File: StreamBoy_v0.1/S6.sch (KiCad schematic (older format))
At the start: 24 parts, among them U1 XC6SLX9-TQG144

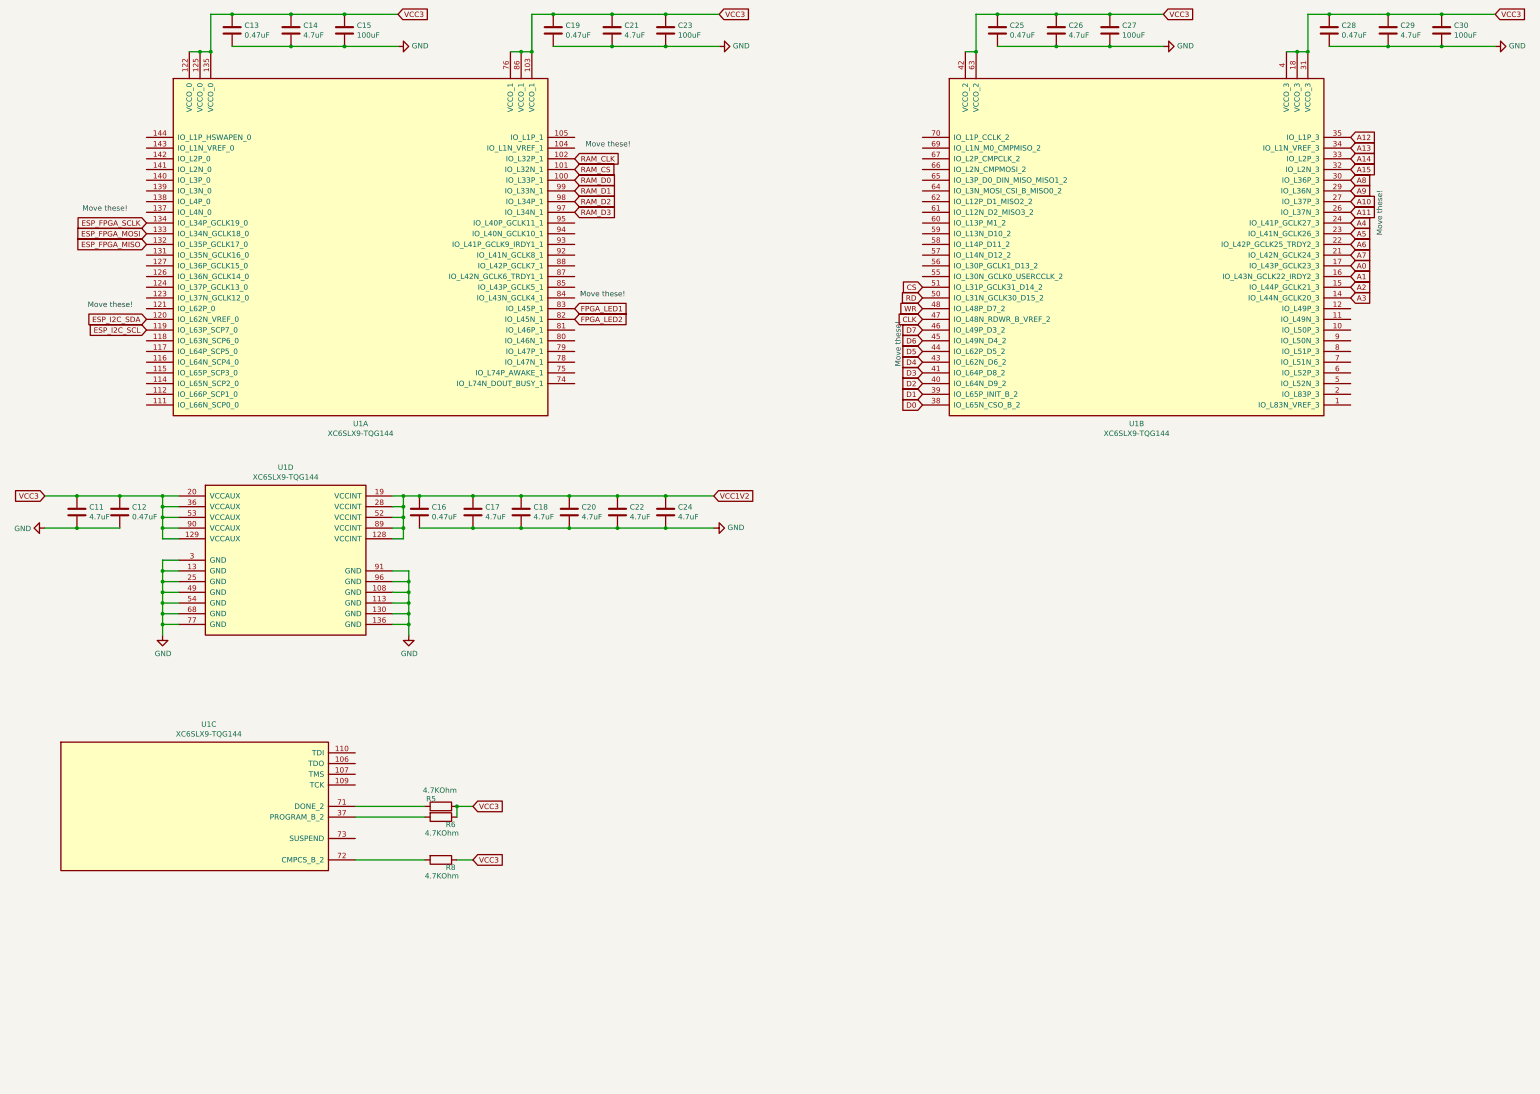
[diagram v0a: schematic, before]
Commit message: Added most stuff to fpga
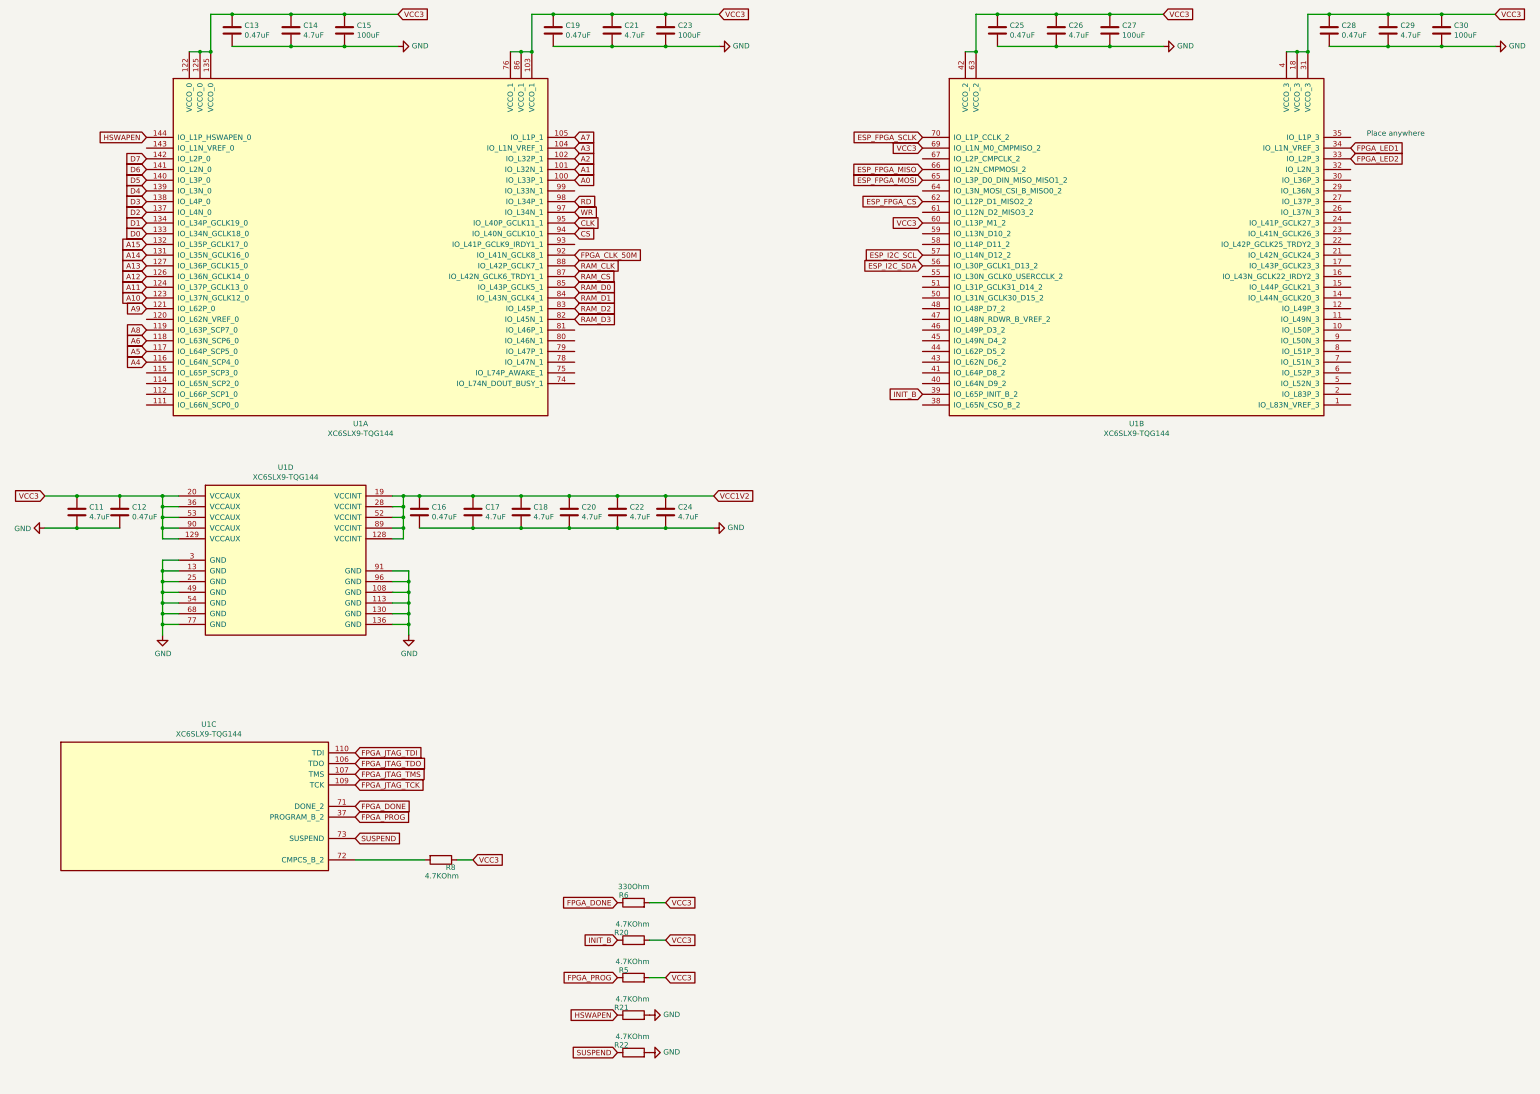
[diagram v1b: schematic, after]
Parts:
- added R20, R21, R22: 4.7KOhm, Resistor_SMD:R_0805_2012Metric, symbol Device:R
- C11, C12, C13, C14, C15, C16, C17, C18, C19, C20, C21, C22, C23, C24, C25, C26, C27, C28, C29, C30: footprint Capacitor_SMD:C_0805_2012Metric -> Capacitor_SMD:C_0402_1005Metric
- R6: value 4.7KOhm -> 330Ohm
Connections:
- net A0: now also U1.100 (IO_L33P_1); no longer U1.17 (IO_L43P_GCLK23_3)
- net A1: now also U1.101 (IO_L32N_1); no longer U1.16 (IO_L43N_GCLK22_IRDY2_3)
- net A10: now also U1.123 (IO_L37N_GCLK12_0); no longer U1.27 (IO_L37P_3)
- net A11: now also U1.124 (IO_L37P_GCLK13_0); no longer U1.26 (IO_L37N_3)
- net A12: now also U1.126 (IO_L36N_GCLK14_0); no longer U1.35 (IO_L1P_3)
- net A13: now also U1.127 (IO_L36P_GCLK15_0); no longer U1.34 (IO_L1N_VREF_3)
- net A14: now also U1.131 (IO_L35N_GCLK16_0); no longer U1.33 (IO_L2P_3)
- net A15: now also U1.132 (IO_L35P_GCLK17_0); no longer U1.32 (IO_L2N_3)
- net A2: now also U1.102 (IO_L32P_1); no longer U1.15 (IO_L44P_GCLK21_3)
- net A3: now also U1.104 (IO_L1N_VREF_1); no longer U1.14 (IO_L44N_GCLK20_3)
- net A4: now also U1.116 (IO_L64N_SCP4_0); no longer U1.24 (IO_L41P_GCLK27_3)
- net A5: now also U1.117 (IO_L64P_SCP5_0); no longer U1.23 (IO_L41N_GCLK26_3)
- net A6: now also U1.118 (IO_L63N_SCP6_0); no longer U1.22 (IO_L42P_GCLK25_TRDY2_3)
- net A7: now also U1.105 (IO_L1P_1); no longer U1.21 (IO_L42N_GCLK24_3)
- net A8: now also U1.119 (IO_L63P_SCP7_0); no longer U1.30 (IO_L36P_3)
- net A9: now also U1.121 (IO_L62P_0); no longer U1.29 (IO_L36N_3)
- net CLK: now also U1.95 (IO_L40P_GCLK11_1); no longer U1.47 (IO_L48N_RDWR_B_VREF_2)
- net CS: now also U1.94 (IO_L40N_GCLK10_1); no longer U1.51 (IO_L31P_GCLK31_D14_2)
- net D0: now also U1.133 (IO_L34N_GCLK18_0); no longer U1.38 (IO_L65N_CSO_B_2)
- net D1: now also U1.134 (IO_L34P_GCLK19_0); no longer U1.39 (IO_L65P_INIT_B_2)
- net D2: now also U1.137 (IO_L4N_0); no longer U1.40 (IO_L64N_D9_2)
- net D3: now also U1.138 (IO_L4P_0); no longer U1.41 (IO_L64P_D8_2)
- net D4: now also U1.139 (IO_L3N_0); no longer U1.43 (IO_L62N_D6_2)
- net D5: now also U1.140 (IO_L3P_0); no longer U1.44 (IO_L62P_D5_2)
- net D6: now also U1.141 (IO_L2N_0); no longer U1.45 (IO_L49N_D4_2)
- net D7: now also U1.142 (IO_L2P_0); no longer U1.46 (IO_L49P_D3_2)
- net ESP_FPGA_MISO: now also U1.66 (IO_L2N_CMPMOSI_2); no longer U1.132 (IO_L35P_GCLK17_0)
- net ESP_FPGA_MOSI: now also U1.65 (IO_L3P_D0_DIN_MISO_MISO1_2); no longer U1.133 (IO_L34N_GCLK18_0)
- net ESP_FPGA_SCLK: now also U1.70 (IO_L1P_CCLK_2); no longer U1.134 (IO_L34P_GCLK19_0)
- net ESP_I2C_SCL: now also U1.57 (IO_L14N_D12_2); no longer U1.119 (IO_L63P_SCP7_0)
- net ESP_I2C_SDA: now also U1.56 (IO_L30P_GCLK1_D13_2); no longer U1.120 (IO_L62N_VREF_0)
- net FPGA_LED1: now also U1.34 (IO_L1N_VREF_3); no longer U1.83 (IO_L45P_1)
- net FPGA_LED2: now also U1.33 (IO_L2P_3); no longer U1.82 (IO_L45N_1)
- net GND: now also R21.2, R22.2
- net RAM_CLK: now also U1.88 (IO_L42P_GCLK7_1); no longer U1.102 (IO_L32P_1)
- net RAM_CS: now also U1.87 (IO_L42N_GCLK6_TRDY1_1); no longer U1.101 (IO_L32N_1)
- net RAM_D0: now also U1.85 (IO_L43P_GCLK5_1); no longer U1.100 (IO_L33P_1)
- net RAM_D1: now also U1.84 (IO_L43N_GCLK4_1); no longer U1.99 (IO_L33N_1)
- net RAM_D2: now also U1.83 (IO_L45P_1); no longer U1.98 (IO_L34P_1)
- net RAM_D3: now also U1.82 (IO_L45N_1); no longer U1.97 (IO_L34N_1)
- net RD: now also U1.98 (IO_L34P_1); no longer U1.50 (IO_L31N_GCLK30_D15_2)
- net VCC3: now also R6.2, U1.60 (IO_L13P_M1_2), U1.69 (IO_L1N_M0_CMPMISO_2), R20.2; no longer R6.1
- net WR: now also U1.97 (IO_L34N_1); no longer U1.48 (IO_L48P_D7_2)
- net HSWAPEN: now reaches U1.144 (IO_L1P_HSWAPEN_0)
- net HSWAPEN: now also R21.1
- net FPGA_CLK_50M: now reaches U1.92 (IO_L41N_GCLK8_1)
- net ESP_FPGA_CS: now reaches U1.62 (IO_L12P_D1_MISO2_2)
- net FPGA_DONE: now reaches U1.71 (DONE_2)
- net FPGA_DONE: now also R6.1; no longer R5.1
- net FPGA_JTAG_TDO: now reaches U1.106 (TDO)
- net FPGA_JTAG_TMS: now reaches U1.107 (TMS)
- net FPGA_JTAG_TCK: now reaches U1.109 (TCK)
- net FPGA_JTAG_TDI: now reaches U1.110 (TDI)
- net FPGA_PROG: now reaches U1.37 (PROGRAM_B_2)
- net FPGA_PROG: now also R5.1; no longer R6.2
- net SUSPEND: now reaches U1.73 (SUSPEND)
- net SUSPEND: now also R22.1
- new net INIT_B: R20.1, U1.39 (IO_L65P_INIT_B_2)
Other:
- note added: "Place anywhere"
- note removed: "Move these!"
- moved on the sheet: R5

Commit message: I hate component placement!
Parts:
- R20, R21, R22, R5, R8: footprint Resistor_SMD:R_0805_2012Metric -> Resistor_SMD:R_0402_1005Metric; lcscPartnum (none) -> C25900
- R6: footprint Resistor_SMD:R_0805_2012Metric -> Resistor_SMD:R_0402_1005Metric; lcscPartnum (none) -> C25890
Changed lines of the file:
@@
 F 0 "R5" V 7070 9746 50  0000 L CNN
 F 1 "4.7KOhm" V 7150 9550 50  0000 L CNN
-F 2 "Resistor_SMD:R_0805_2012Metric" V 6930 9700 50  0001 C CNN
+F 2 "Resistor_SMD:R_0402_1005Metric" V 6930 9700 50  0001 C CNN
 F 3 "~" H 7000 9700 50  0001 C CNN
+F 4 "C25900" H 7000 9700 50  0001 C CNN "lcscPartnum"
 	1    7000 9700
 	0    -1   -1   0
@@
 F 0 "R8" V 5270 8646 50  0000 L CNN
 F 1 "4.7KOhm" V 5350 8450 50  0000 L CNN
-F 2 "Resistor_SMD:R_0805_2012Metric" V 5130 8600 50  0001 C CNN
+F 2 "Resistor_SMD:R_0402_1005Metric" V 5130 8600 50  0001 C CNN
 F 3 "~" H 5200 8600 50  0001 C CNN
+F 4 "C25900" H 5200 8600 50  0001 C CNN "lcscPartnum"
 	1    5200 8600
 	0    1    1    0
@@
 F 0 "R20" V 7070 9396 50  0000 L CNN
 F 1 "4.7KOhm" V 7150 9200 50  0000 L CNN
-F 2 "Resistor_SMD:R_0805_2012Metric" V 6930 9350 50  0001 C CNN
+F 2 "Resistor_SMD:R_0402_1005Metric" V 6930 9350 50  0001 C CNN
 F 3 "~" H 7000 9350 50  0001 C CNN
+F 4 "C25900" H 7000 9350 50  0001 C CNN "lcscPartnum"
 	1    7000 9350
 	0    -1   -1   0
@@
 F 0 "R6" V 7070 9046 50  0000 L CNN
 F 1 "330Ohm" V 7150 8850 50  0000 L CNN
-F 2 "Resistor_SMD:R_0805_2012Metric" V 6930 9000 50  0001 C CNN
+F 2 "Resistor_SMD:R_0402_1005Metric" V 6930 9000 50  0001 C CNN
 F 3 "~" H 7000 9000 50  0001 C CNN
+F 4 "C25890" H 7000 9000 50  0001 C CNN "lcscPartnum"
 	1    7000 9000
 	0    -1   -1   0
@@
 F 0 "R21" V 7070 10096 50  0000 L CNN
 F 1 "4.7KOhm" V 7150 9900 50  0000 L CNN
-F 2 "Resistor_SMD:R_0805_2012Metric" V 6930 10050 50  0001 C CNN
+F 2 "Resistor_SMD:R_0402_1005Metric" V 6930 10050 50  0001 C CNN
 F 3 "~" H 7000 10050 50  0001 C CNN
+F 4 "C25900" H 7000 10050 50  0001 C CNN "lcscPartnum"
 	1    7000 10050
 	0    -1   -1   0
@@
 F 0 "R22" V 7070 10446 50  0000 L CNN
 F 1 "4.7KOhm" V 7150 10250 50  0000 L CNN
-F 2 "Resistor_SMD:R_0805_2012Metric" V 6930 10400 50  0001 C CNN
+F 2 "Resistor_SMD:R_0402_1005Metric" V 6930 10400 50  0001 C CNN
 F 3 "~" H 7000 10400 50  0001 C CNN
+F 4 "C25900" H 7000 10400 50  0001 C CNN "lcscPartnum"
 	1    7000 10400
 	0    -1   -1   0

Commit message: Started to route some stuff
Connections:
- net A4: now also U1.115 (IO_L65P_SCP3_0); no longer U1.116 (IO_L64N_SCP4_0)
- net A5: now also U1.116 (IO_L64N_SCP4_0); no longer U1.117 (IO_L64P_SCP5_0)
- net A6: now also U1.117 (IO_L64P_SCP5_0); no longer U1.118 (IO_L63N_SCP6_0)
- net A7: now also U1.118 (IO_L63N_SCP6_0); no longer U1.105 (IO_L1P_1)
- net RAM_D0: now also U1.82 (IO_L45N_1); no longer U1.85 (IO_L43P_GCLK5_1)
- net RAM_D2: now also U1.85 (IO_L43P_GCLK5_1); no longer U1.83 (IO_L45P_1)
- net RAM_D3: now also U1.83 (IO_L45P_1); no longer U1.82 (IO_L45N_1)
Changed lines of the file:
@@
 Text GLabel 6450 3150 2    50   Input ~ 0
 RAM_CS
-Text GLabel 6450 3250 2    50   Input ~ 0
+Text GLabel 6450 3550 2    50   Input ~ 0
 RAM_D0
 Text GLabel 6450 3350 2    50   Input ~ 0
 RAM_D1
+Text GLabel 6450 3250 2    50   Input ~ 0
+RAM_D2
 Text GLabel 6450 3450 2    50   Input ~ 0
-RAM_D2
-Text GLabel 6450 3550 2    50   Input ~ 0
 RAM_D3
 Text GLabel 13700 1950 2    50   Input ~ 0
@@
 Text GLabel 13700 2050 2    50   Input ~ 0
 FPGA_LED2
+Text GLabel 2450 4050 0    50   Input ~ 0
+A4
 Text GLabel 2450 3950 0    50   Input ~ 0
-A4
+A5
 Text GLabel 2450 3850 0    50   Input ~ 0
-A5
-Text GLabel 2450 3750 0    50   Input ~ 0
 A6
 Text GLabel 2450 3650 0    50   Input ~ 0
@@
 Text Notes 13850 1850 0    50   ~ 0
 Place anywhere
-Text GLabel 6450 1850 2    50   Input ~ 0
+Text GLabel 2450 3750 0    50   Input ~ 0
 A7
 Text GLabel 6450 1950 2    50   Input ~ 0

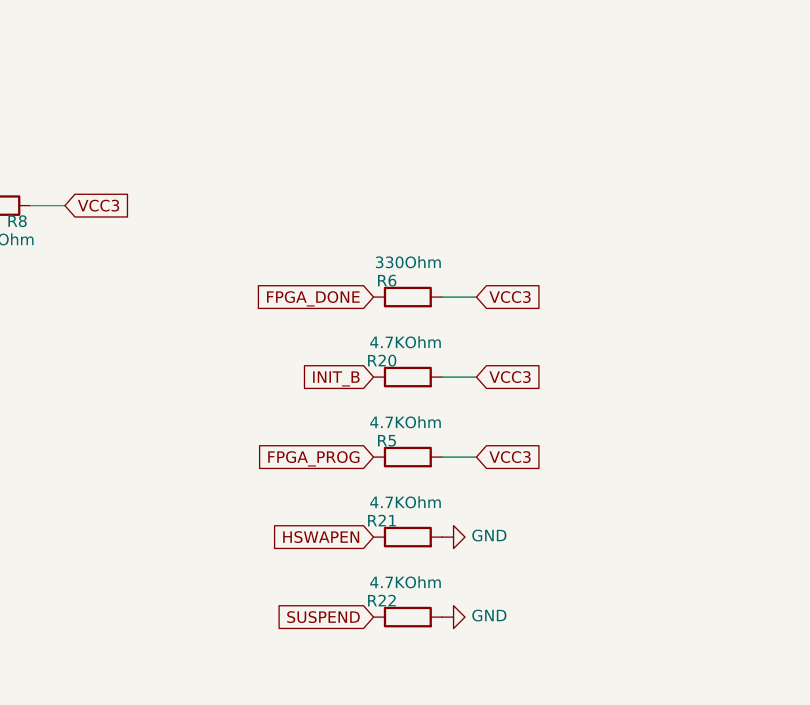
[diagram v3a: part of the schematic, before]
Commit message: GB Reset fixed and moved some stuff
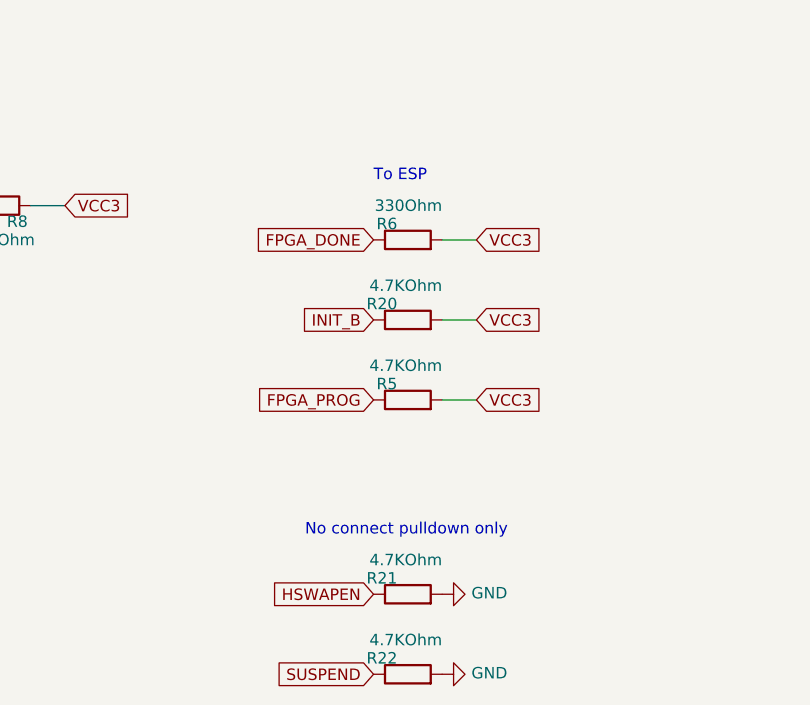
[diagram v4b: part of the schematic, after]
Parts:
- C11, C14, C17, C18, C20, C21, C22, C24, C26, C29: lcscPartnum (none) -> C23733
- C12, C13, C16, C19, C25, C28: lcscPartnum (none) -> C47339
- C15, C23, C27, C30: footprint Capacitor_SMD:C_0402_1005Metric -> Capacitor_SMD:C_1206_3216Metric; lcscPartnum (none) -> C15008
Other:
- note added: "No connect pulldown only"
- note added: "To ESP"
- moved on the sheet: R20, R21, R22, R5, R6
